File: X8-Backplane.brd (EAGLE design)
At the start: 122.1 x 122.1 mm, 0 parts

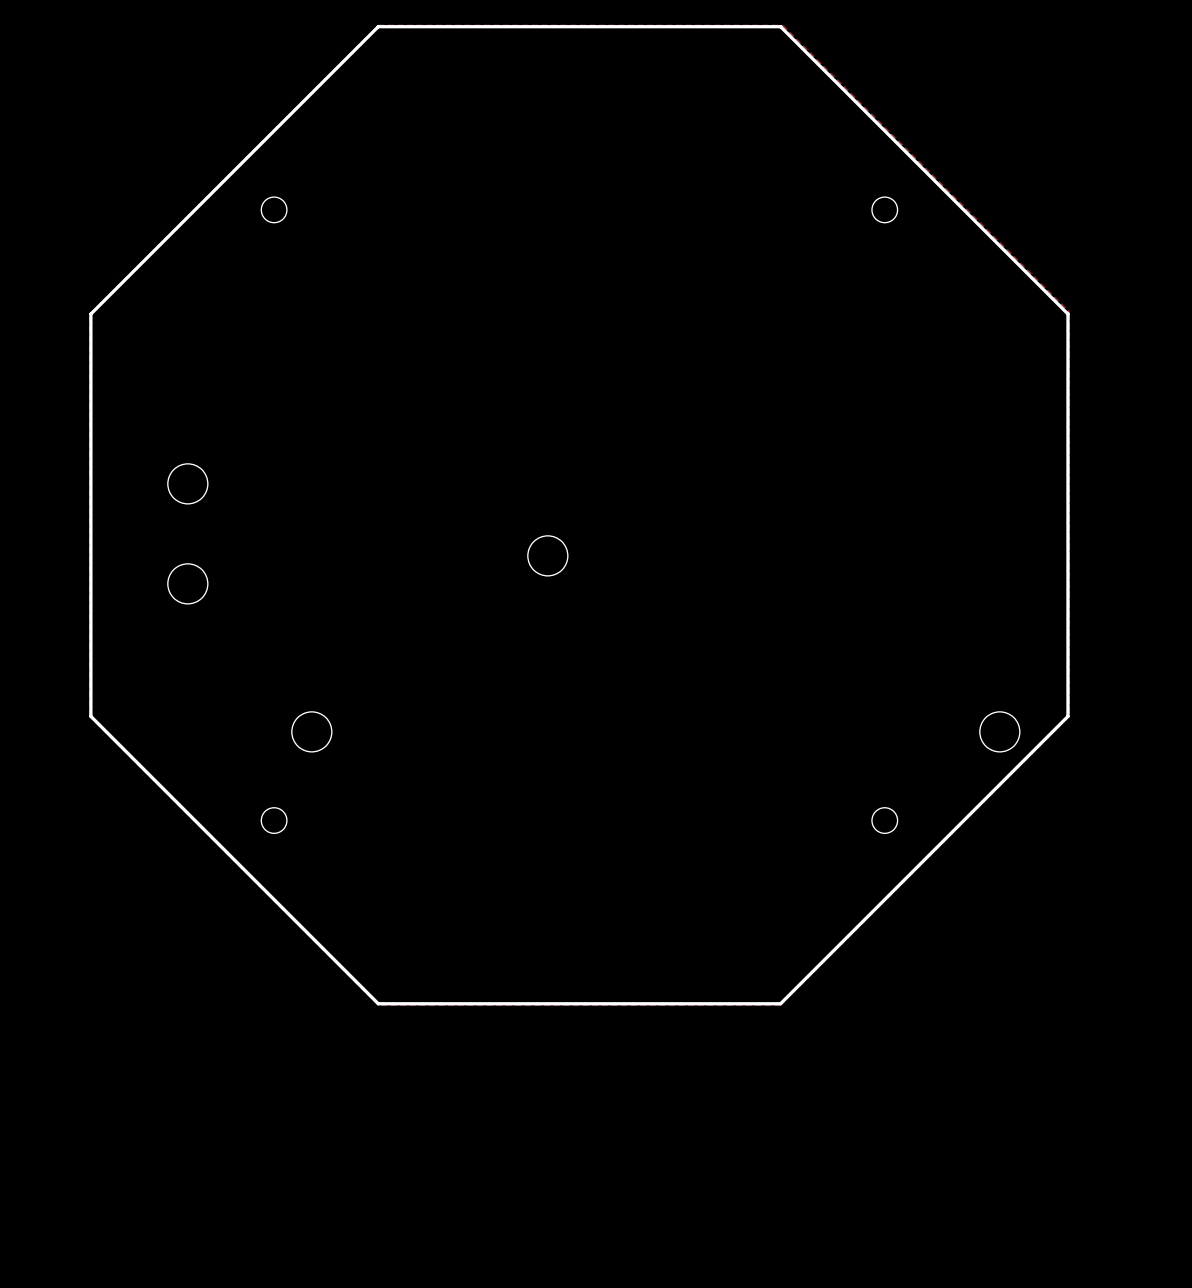
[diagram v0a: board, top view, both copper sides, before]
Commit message: Added part for raspberry pi, 5V -> 3.3V buck converter, and IMU pins
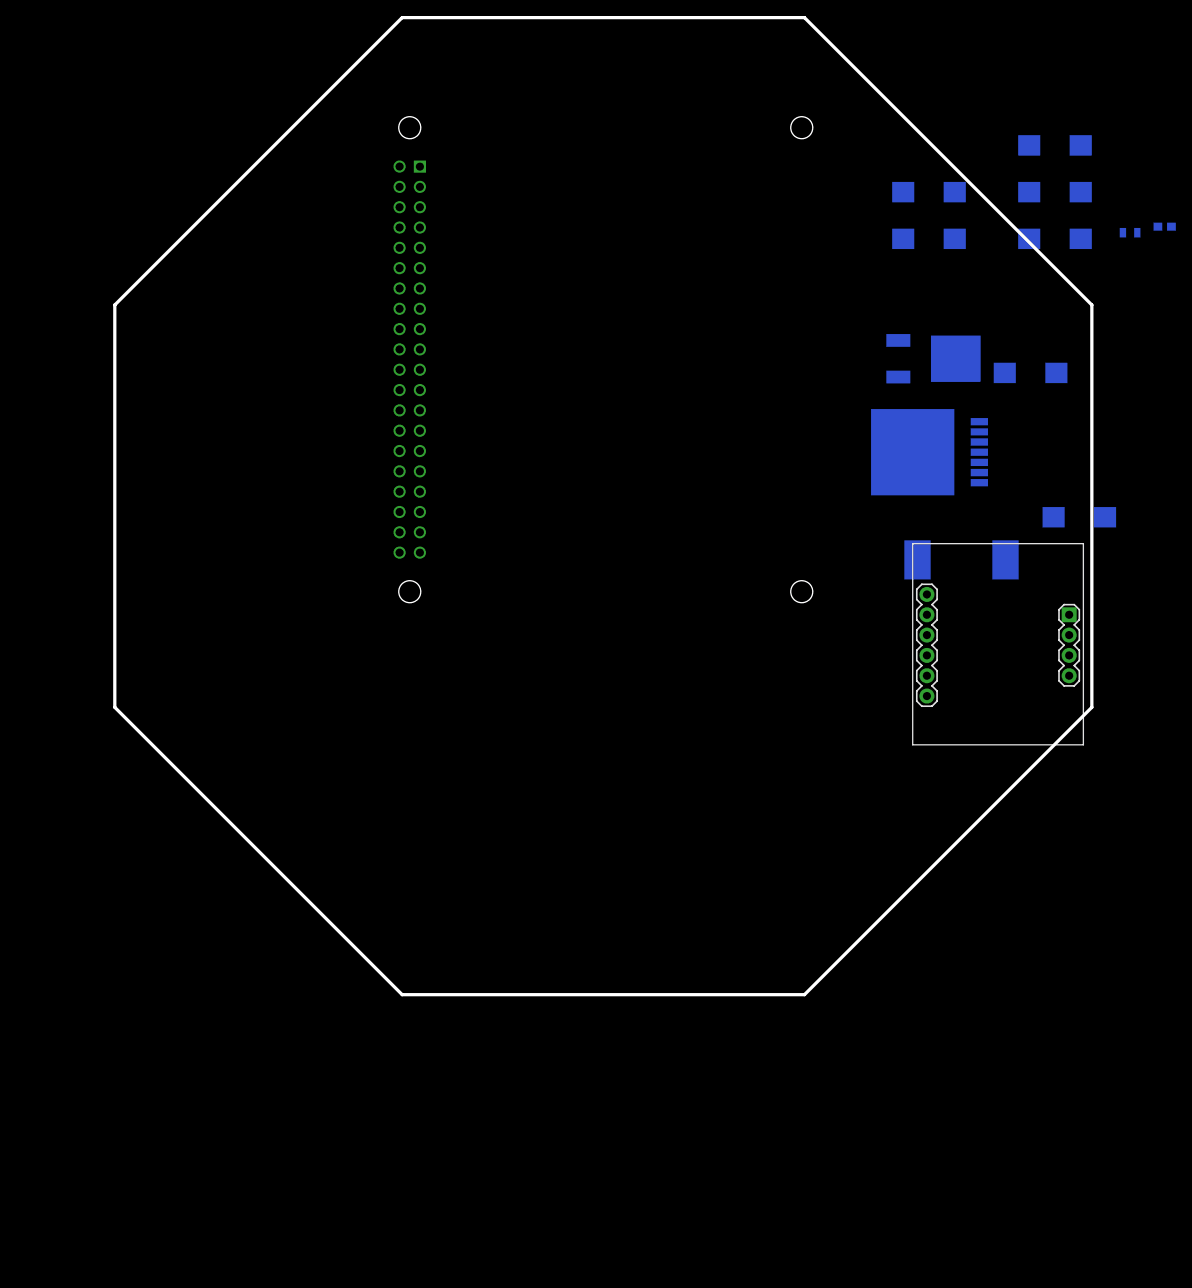
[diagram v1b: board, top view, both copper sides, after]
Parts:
- added C10, C6, C9: 150uF, PowerComponents:CTAN(7.30_4.30MM)
- added C11, C12, C13, C2: 10uF, PowerComponents:CTAN(7.30_4.30MM)
- added C3: 0.47uF, SparkFun-Capacitors:0805
- added C4: 0.01uF, SparkFun-Passives:0603-CAP
- added PCB1: RPI2, MicrocontrollerComponents:RPI2
- added U$1: SWITCHMODE_SCHOTTKY, PowerComponents:DPAK-3
- added U$2: 15uH, DiscreteComponents:HCMA1305
- added U$3: BNO055_9DOF_BREAKOUT, Other:BNO055
- added U1: LM2678, PowerComponents:LM2678
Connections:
- new net +12V: C11.+, C12.+, C13.+, C2.+, C3.1, U1.2
- new net +5V: C10.+, C6.+, C9.+, U$2.P$2, U1.6
- new net GND: C10.-, C11.-, C12.-, C13.-, C2.-, C3.2, C6.-, C9.-, U$1.P$1, U$1.P$3, U1.4, U1.TAB
- new net N$2: C4.1, U1.3
- new net N$3: C4.2, U$1.P$4, U$2.P$1, U1.1
- new net N$4: PCB1.P$1
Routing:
- removed copper zone on layer 1, net GND
- removed copper zone on layer 16, net GND

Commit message: small modification to outline
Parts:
- moved U$3 93.0 mm to (19.8, 21.1), turned to 270 degrees
- moved U$2 4.68 mm to (107.2, 26.9)
- moved PCB1 1.52 mm to (90.2, 89.0)
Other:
- board size 122.1 x 122.1 mm -> 122.1 x 106.6 mm
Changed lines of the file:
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@@
 <circle x="63.43686875" y="38.21558125" radius="73.025" width="0.4064" layer="51"/>
 <wire x1="38.29215" y1="99.28131875" x2="2.371125" y2="63.36029375" width="0.4064" layer="20"/>
-<wire x1="124.50260625" y1="13.0708625" x2="88.581584375" y2="-22.8501625" width="0.4064" layer="20"/>
-<wire x1="2.371125" y1="13.0708625" x2="38.29215" y2="-22.8501625" width="0.4064" layer="20"/>
+<wire x1="124.50260625" y1="13.0708625" x2="103.567584375" y2="-7.3561625" width="0.4064" layer="20"/>
+<wire x1="2.371125" y1="13.0708625" x2="22.29015" y2="-7.3561625" width="0.4064" layer="20"/>
 <wire x1="88.581584375" y1="99.28131875" x2="124.50260625" y2="63.36029375" width="0.4064" layer="20"/>
 <wire x1="88.581584375" y1="99.28131875" x2="38.29215" y2="99.28131875" width="0.4064" layer="20"/>
 <wire x1="124.50260625" y1="63.36029375" x2="124.50260625" y2="13.0708625" width="0.4064" layer="20"/>
-<wire x1="88.581584375" y1="-22.8501625" x2="38.29215" y2="-22.8501625" width="0.4064" layer="20"/>
 <wire x1="2.371125" y1="63.36029375" x2="2.371125" y2="13.0708625" width="0.4064" layer="20"/>
+<wire x1="22.352" y1="-7.366" x2="103.378" y2="-7.366" width="0.4064" layer="20" curve="-104.736525"/>
 </plain>
 <attributes>
@@
 </autorouter>
 <elements>
-<element name="PCB1" library="MicrocontrollerComponents" package="RPI2" value="RPI2" x="91.74" y="89.022" rot="MR270"/>
+<element name="PCB1" library="MicrocontrollerComponents" package="RPI2" value="RPI2" x="90.216" y="89.022" rot="MR270"/>
 <element name="U$1" library="PowerComponents" package="DPAK-3" value="SWITCHMODE_SCHOTTKY" x="104.394" y="56.642" rot="MR0"/>
 <element name="U1" library="PowerComponents" package="LM2678" value="LM2678" x="102.108" y="44.958" rot="MR180"/>
 <element name="C3" library="SparkFun-Capacitors" package="0805" value="0.47uF" x="129.286" y="72.39" rot="MR0"/>
 <element name="C4" library="SparkFun-Passives" package="0603-CAP" value="0.01uF" x="133.604" y="73.152" rot="MR0"/>
-<element name="U$2" library="DiscreteComponents" package="HCMA1305" value="15uH" x="108.204" y="31.496" rot="MR90"/>
+<element name="U$2" library="DiscreteComponents" package="HCMA1305" value="15uH" x="107.188" y="26.924" rot="MR90"/>
 <element name="C6" library="PowerComponents" package="CTAN(7.30_4.30MM)" value="150uF" x="122.936" y="36.83" rot="MR0"/>
 <element name="C9" library="PowerComponents" package="CTAN(7.30_4.30MM)" value="150uF" x="119.888" y="83.312" rot="MR0"/>
@@
 <element name="C13" library="PowerComponents" package="CTAN(7.30_4.30MM)" value="10uF" x="119.888" y="71.628" rot="MR0"/>
 <element name="C2" library="PowerComponents" package="CTAN(7.30_4.30MM)" value="10uF" x="116.84" y="54.864" rot="MR180"/>
-<element name="U$3" library="Other" package="BNO055" value="BNO055_9DOF_BREAKOUT" x="112.776" y="22.098"/>
+<element name="U$3" library="Other" package="BNO055" value="BNO055_9DOF_BREAKOUT" x="19.812" y="21.082" rot="R270"/>
 </elements>
 <signals>
@@
 <contactref element="U$1" pad="P$4"/>
 <wire x1="110.4392" y1="48.768" x2="107.494" y2="56.642" width="0" layer="19" extent="1-1"/>
-<wire x1="113.704" y1="31.496" x2="110.4392" y2="48.768" width="0" layer="19" extent="1-1"/>
+<wire x1="112.688" y1="26.924" x2="110.4392" y2="48.768" width="0" layer="19" extent="1-1"/>
 <wire x1="132.754" y1="73.152" x2="107.494" y2="56.642" width="0" layer="19" extent="1-1"/>
 </signal>
@@
 <wire x1="123.108" y1="83.312" x2="126.156" y2="36.83" width="0" layer="19" extent="1-1"/>
 <wire x1="110.4392" y1="42.418" x2="123.108" y2="83.312" width="0" layer="19" extent="1-1"/>
-<wire x1="102.704" y1="31.496" x2="110.4392" y2="42.418" width="0" layer="19" extent="1-1"/>
+<wire x1="101.688" y1="26.924" x2="110.4392" y2="42.418" width="0" layer="19" extent="1-1"/>
 </signal>
 <signal name="N$4">

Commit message: Intermediate layout
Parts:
- moved C4 55.0 mm to (104.1, 26.7), turned to 180 degrees
- moved C6 51.8 mm to (90.4, 77.2), turned to 180 degrees
- moved U$2 37.6 mm to (83.6, 56.1)
- moved C11 34.8 mm to (98.8, 49.8), turned to 270 degrees
- moved C9 34.4 mm to (90.4, 65.5), turned to 180 degrees
- moved C3 30.8 mm to (109.2, 49.0), turned to 270 degrees
- moved C13 26.6 mm to (104.6, 49.8), turned to 270 degrees
- moved U$1 21.5 mm to (87.9, 42.9), turned to 270 degrees
- moved C10 15.0 mm to (90.4, 71.4), turned to 180 degrees
- moved C2 13.4 mm to (104.6, 60.5), turned to 90 degrees
- moved C12 12.4 mm to (98.8, 60.5), turned to 90 degrees
- moved U1 6.40 mm to (101.3, 38.6), turned to 270 degrees
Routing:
- added copper zone on layer 16, net +12V
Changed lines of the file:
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@@
 <layer number="49" name="Reference" color="7" fill="1" visible="yes" active="yes"/>
 <layer number="50" name="dxf" color="7" fill="1" visible="no" active="no"/>
-<layer number="51" name="tDocu" color="7" fill="1" visible="yes" active="yes"/>
+<layer number="51" name="tDocu" color="7" fill="1" visible="no" active="yes"/>
 <layer number="52" name="bDocu" color="7" fill="1" visible="yes" active="yes"/>
 <layer number="53" name="tGND_GNDA" color="7" fill="1" visible="no" active="no"/>
@@
 <elements>
 <element name="PCB1" library="MicrocontrollerComponents" package="RPI2" value="RPI2" x="90.216" y="89.022" rot="MR270"/>
-<element name="U$1" library="PowerComponents" package="DPAK-3" value="SWITCHMODE_SCHOTTKY" x="104.394" y="56.642" rot="MR0"/>
-<element name="U1" library="PowerComponents" package="LM2678" value="LM2678" x="102.108" y="44.958" rot="MR180"/>
-<element name="C3" library="SparkFun-Capacitors" package="0805" value="0.47uF" x="129.286" y="72.39" rot="MR0"/>
-<element name="C4" library="SparkFun-Passives" package="0603-CAP" value="0.01uF" x="133.604" y="73.152" rot="MR0"/>
-<element name="U$2" library="DiscreteComponents" package="HCMA1305" value="15uH" x="107.188" y="26.924" rot="MR90"/>
-<element name="C6" library="PowerComponents" package="CTAN(7.30_4.30MM)" value="150uF" x="122.936" y="36.83" rot="MR0"/>
-<element name="C9" library="PowerComponents" package="CTAN(7.30_4.30MM)" value="150uF" x="119.888" y="83.312" rot="MR0"/>
-<element name="C10" library="PowerComponents" package="CTAN(7.30_4.30MM)" value="150uF" x="104.14" y="77.47" rot="MR0"/>
-<element name="C11" library="PowerComponents" package="CTAN(7.30_4.30MM)" value="10uF" x="119.888" y="77.47" rot="MR0"/>
-<element name="C12" library="PowerComponents" package="CTAN(7.30_4.30MM)" value="10uF" x="104.14" y="71.628" rot="MR0"/>
-<element name="C13" library="PowerComponents" package="CTAN(7.30_4.30MM)" value="10uF" x="119.888" y="71.628" rot="MR0"/>
-<element name="C2" library="PowerComponents" package="CTAN(7.30_4.30MM)" value="10uF" x="116.84" y="54.864" rot="MR180"/>
+<element name="U$1" library="PowerComponents" package="DPAK-3" value="SWITCHMODE_SCHOTTKY" x="87.884" y="42.926" rot="MR270"/>
+<element name="U1" library="PowerComponents" package="LM2678" value="LM2678" x="101.346" y="38.608" rot="MR270"/>
+<element name="C3" library="SparkFun-Capacitors" package="0805" value="0.47uF" x="109.22" y="49.022" rot="MR270"/>
+<element name="C4" library="SparkFun-Passives" package="0603-CAP" value="0.01uF" x="104.14" y="26.67" rot="MR180"/>
+<element name="U$2" library="DiscreteComponents" package="HCMA1305" value="15uH" x="83.566" y="56.134" rot="MR90"/>
+<element name="C6" library="PowerComponents" package="CTAN(7.30_4.30MM)" value="150uF" x="90.424" y="77.216" rot="MR180"/>
+<element name="C9" library="PowerComponents" package="CTAN(7.30_4.30MM)" value="150uF" x="90.424" y="65.532" rot="MR180"/>
+<element name="C10" library="PowerComponents" package="CTAN(7.30_4.30MM)" value="150uF" x="90.424" y="71.374" rot="MR180"/>
+<element name="C11" library="PowerComponents" package="CTAN(7.30_4.30MM)" value="10uF" x="98.806" y="49.784" rot="MR270"/>
+<element name="C12" library="PowerComponents" package="CTAN(7.30_4.30MM)" value="10uF" x="98.806" y="60.452" rot="MR90"/>
+<element name="C13" library="PowerComponents" package="CTAN(7.30_4.30MM)" value="10uF" x="104.648" y="49.784" rot="MR270"/>
+<element name="C2" library="PowerComponents" package="CTAN(7.30_4.30MM)" value="10uF" x="104.648" y="60.452" rot="MR90"/>
 <element name="U$3" library="Other" package="BNO055" value="BNO055_9DOF_BREAKOUT" x="19.812" y="21.082" rot="R270"/>
 </elements>
@@
 <contactref element="U1" pad="3"/>
 <contactref element="C4" pad="1"/>
-<wire x1="110.4392" y1="46.228" x2="134.454" y2="73.152" width="0" layer="19" extent="1-1"/>
+<wire x1="103.29" y1="26.67" x2="102.616" y2="30.2768" width="0" layer="19" extent="16-16"/>
 </signal>
 <signal name="N$3">
@@
 <contactref element="U$2" pad="P$1"/>
 <contactref element="U$1" pad="P$4"/>
-<wire x1="110.4392" y1="48.768" x2="107.494" y2="56.642" width="0" layer="19" extent="1-1"/>
-<wire x1="112.688" y1="26.924" x2="110.4392" y2="48.768" width="0" layer="19" extent="1-1"/>
-<wire x1="132.754" y1="73.152" x2="107.494" y2="56.642" width="0" layer="19" extent="1-1"/>
+<wire x1="87.884" y1="46.026" x2="89.066" y2="56.134" width="0" layer="19" extent="16-16"/>
+<wire x1="105.156" y1="30.2768" x2="87.884" y2="46.026" width="0" layer="19" extent="16-16"/>
+<wire x1="104.99" y1="26.67" x2="105.156" y2="30.2768" width="0" layer="19" extent="16-16"/>
 </signal>
 <signal name="GND">
@@
 <contactref element="C2" pad="-"/>
 <contactref element="C12" pad="-"/>
-<wire x1="116.668" y1="77.47" x2="116.668" y2="83.312" width="0" layer="19" extent="1-1"/>
-<wire x1="116.668" y1="71.628" x2="116.668" y2="77.47" width="0" layer="19" extent="1-1"/>
-<wire x1="128.386" y1="72.39" x2="116.668" y2="71.628" width="0" layer="19" extent="1-1"/>
-<wire x1="100.92" y1="77.47" x2="116.668" y2="77.47" width="0" layer="19" extent="1-1"/>
-<wire x1="100.92" y1="71.628" x2="100.92" y2="77.47" width="0" layer="19" extent="1-1"/>
-<wire x1="100.314" y1="58.927" x2="100.92" y2="71.628" width="0" layer="19" extent="1-1"/>
-<wire x1="100.314" y1="54.357" x2="100.314" y2="58.927" width="0" layer="19" extent="1-1"/>
-<wire x1="110.4392" y1="44.958" x2="100.314" y2="54.357" width="0" layer="19" extent="1-1"/>
-<wire x1="102.108" y1="44.958" x2="110.4392" y2="44.958" width="0" layer="19" extent="1-1"/>
-<wire x1="119.716" y1="36.83" x2="110.4392" y2="44.958" width="0" layer="19" extent="1-1"/>
-<wire x1="120.06" y1="54.864" x2="119.716" y2="36.83" width="0" layer="19" extent="1-1"/>
+<wire x1="98.806" y1="63.672" x2="104.648" y2="63.672" width="0" layer="19" extent="16-16"/>
+<wire x1="93.644" y1="65.532" x2="98.806" y2="63.672" width="0" layer="19" extent="16-16"/>
+<wire x1="93.644" y1="71.374" x2="93.644" y2="65.532" width="0" layer="19" extent="16-16"/>
+<wire x1="93.644" y1="77.216" x2="93.644" y2="71.374" width="0" layer="19" extent="16-16"/>
+<wire x1="109.22" y1="48.122" x2="104.648" y2="63.672" width="0" layer="19" extent="16-16"/>
+<wire x1="104.648" y1="46.564" x2="109.22" y2="48.122" width="0" layer="19" extent="16-16"/>
+<wire x1="98.806" y1="46.564" x2="104.648" y2="46.564" width="0" layer="19" extent="16-16"/>
+<wire x1="101.346" y1="38.608" x2="98.806" y2="46.564" width="0" layer="19" extent="16-16"/>
+<wire x1="90.169" y1="38.846" x2="101.346" y2="38.608" width="0" layer="19" extent="16-16"/>
+<wire x1="85.599" y1="38.846" x2="90.169" y2="38.846" width="0" layer="19" extent="16-16"/>
+<wire x1="101.346" y1="30.2768" x2="101.346" y2="38.608" width="0" layer="19" extent="16-16"/>
 </signal>
 <signal name="+12V">
@@
 <contactref element="C2" pad="+"/>
 <contactref element="C12" pad="+"/>
-<wire x1="123.108" y1="71.628" x2="107.36" y2="71.628" width="0" layer="19" extent="1-1"/>
-<wire x1="123.108" y1="77.47" x2="123.108" y2="71.628" width="0" layer="19" extent="1-1"/>
-<wire x1="130.186" y1="72.39" x2="123.108" y2="71.628" width="0" layer="19" extent="1-1"/>
-<wire x1="113.62" y1="54.864" x2="123.108" y2="77.47" width="0" layer="19" extent="1-1"/>
-<wire x1="110.4392" y1="47.498" x2="113.62" y2="54.864" width="0" layer="19" extent="1-1"/>
+<polygon width="0.4064" layer="16">
+<vertex x="97.028" y="58.928"/>
+<vertex x="112.014" y="58.928"/>
+<vertex x="112.014" y="51.054"/>
+<vertex x="112.014" y="49.784"/>
+<vertex x="97.028" y="49.784"/>
+</polygon>
+<wire x1="109.22" y1="49.922" x2="103.886" y2="30.2768" width="0" layer="19" extent="16-16"/>
 </signal>
 <signal name="+5V">
@@
 <contactref element="C9" pad="+"/>
 <contactref element="C10" pad="+"/>
-<wire x1="126.156" y1="36.83" x2="107.36" y2="77.47" width="0" layer="19" extent="1-1"/>
-<wire x1="123.108" y1="83.312" x2="126.156" y2="36.83" width="0" layer="19" extent="1-1"/>
-<wire x1="110.4392" y1="42.418" x2="123.108" y2="83.312" width="0" layer="19" extent="1-1"/>
-<wire x1="101.688" y1="26.924" x2="110.4392" y2="42.418" width="0" layer="19" extent="1-1"/>
+<wire x1="87.204" y1="71.374" x2="87.204" y2="77.216" width="0" layer="19" extent="16-16"/>
+<wire x1="87.204" y1="65.532" x2="87.204" y2="71.374" width="0" layer="19" extent="16-16"/>
+<wire x1="78.066" y1="56.134" x2="87.204" y2="65.532" width="0" layer="19" extent="16-16"/>
+<wire x1="98.806" y1="30.2768" x2="78.066" y2="56.134" width="0" layer="19" extent="16-16"/>
 </signal>
 <signal name="N$4">
